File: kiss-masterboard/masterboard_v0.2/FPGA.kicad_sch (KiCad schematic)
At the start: 68 parts, among them J10 CRESET, J11 Jumper, J12 Jumper, J13 Conn_02x08_Odd_Even, J14 Conn_02x08_Odd_Even, J15 jmp, J16 jmp, J8 Jumper, J9 jmp, U12 1V2, U13 SN74LVC8T245, U14 W25Q, U17 12MHz, U2 SN74LVC8T245, U3 3.3V, U4 ICE40UP5k-SG48, U5 SN74LVC8T245

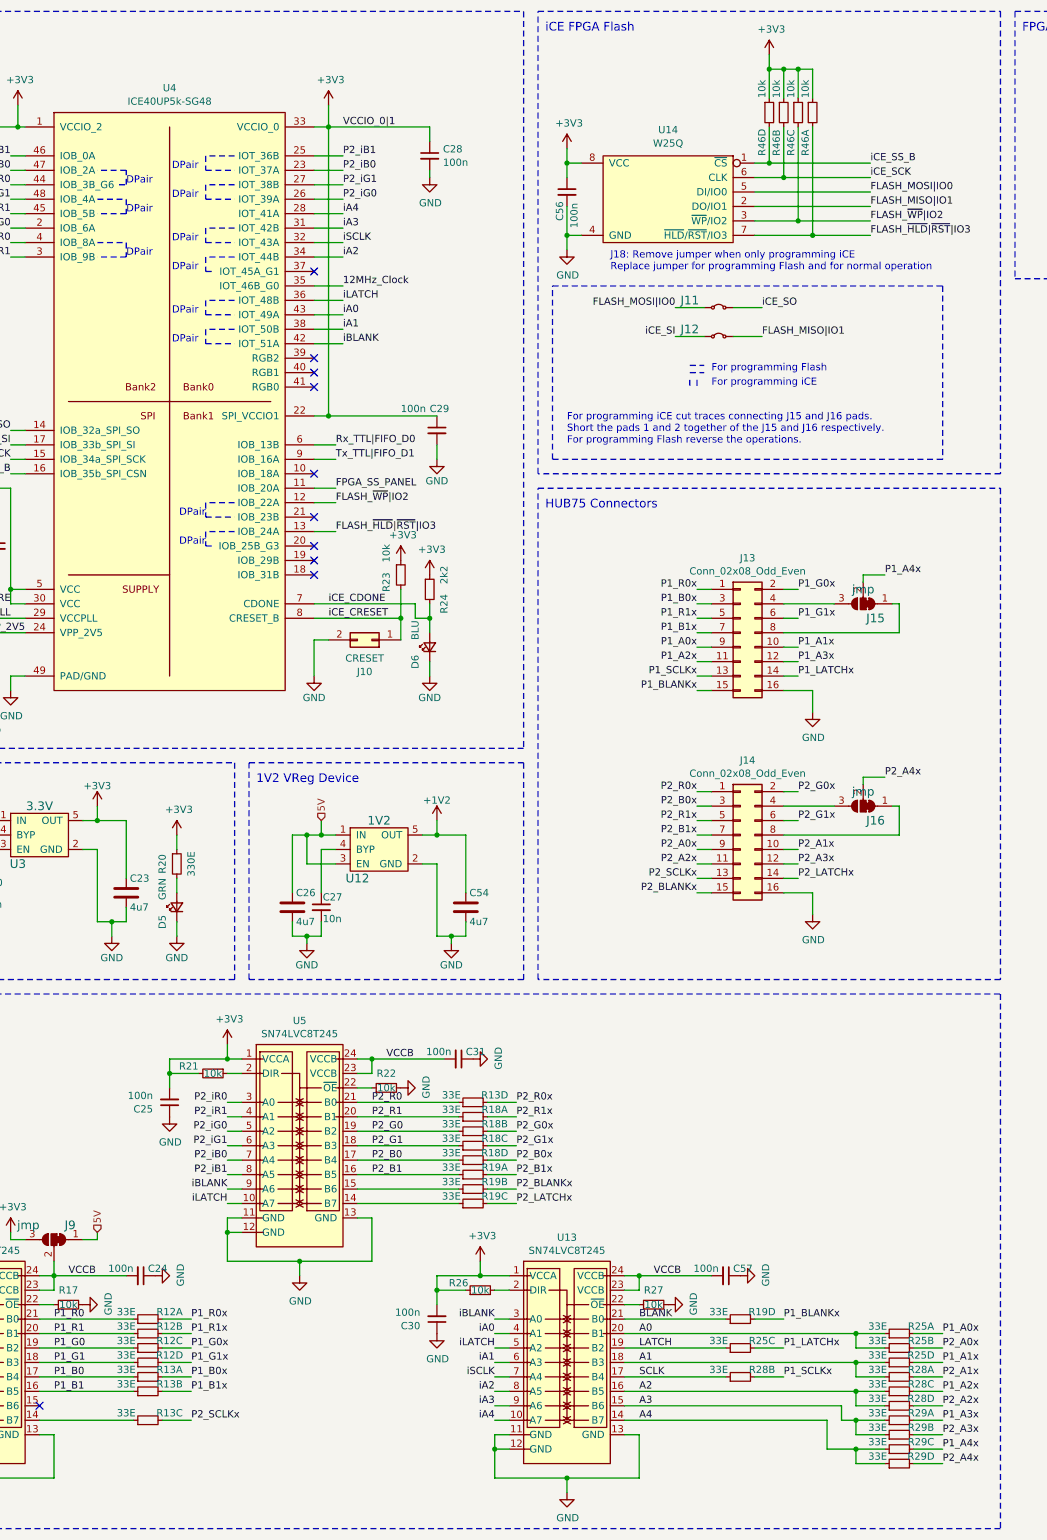
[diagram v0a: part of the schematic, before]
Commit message: replaced resistor array with normal resistors
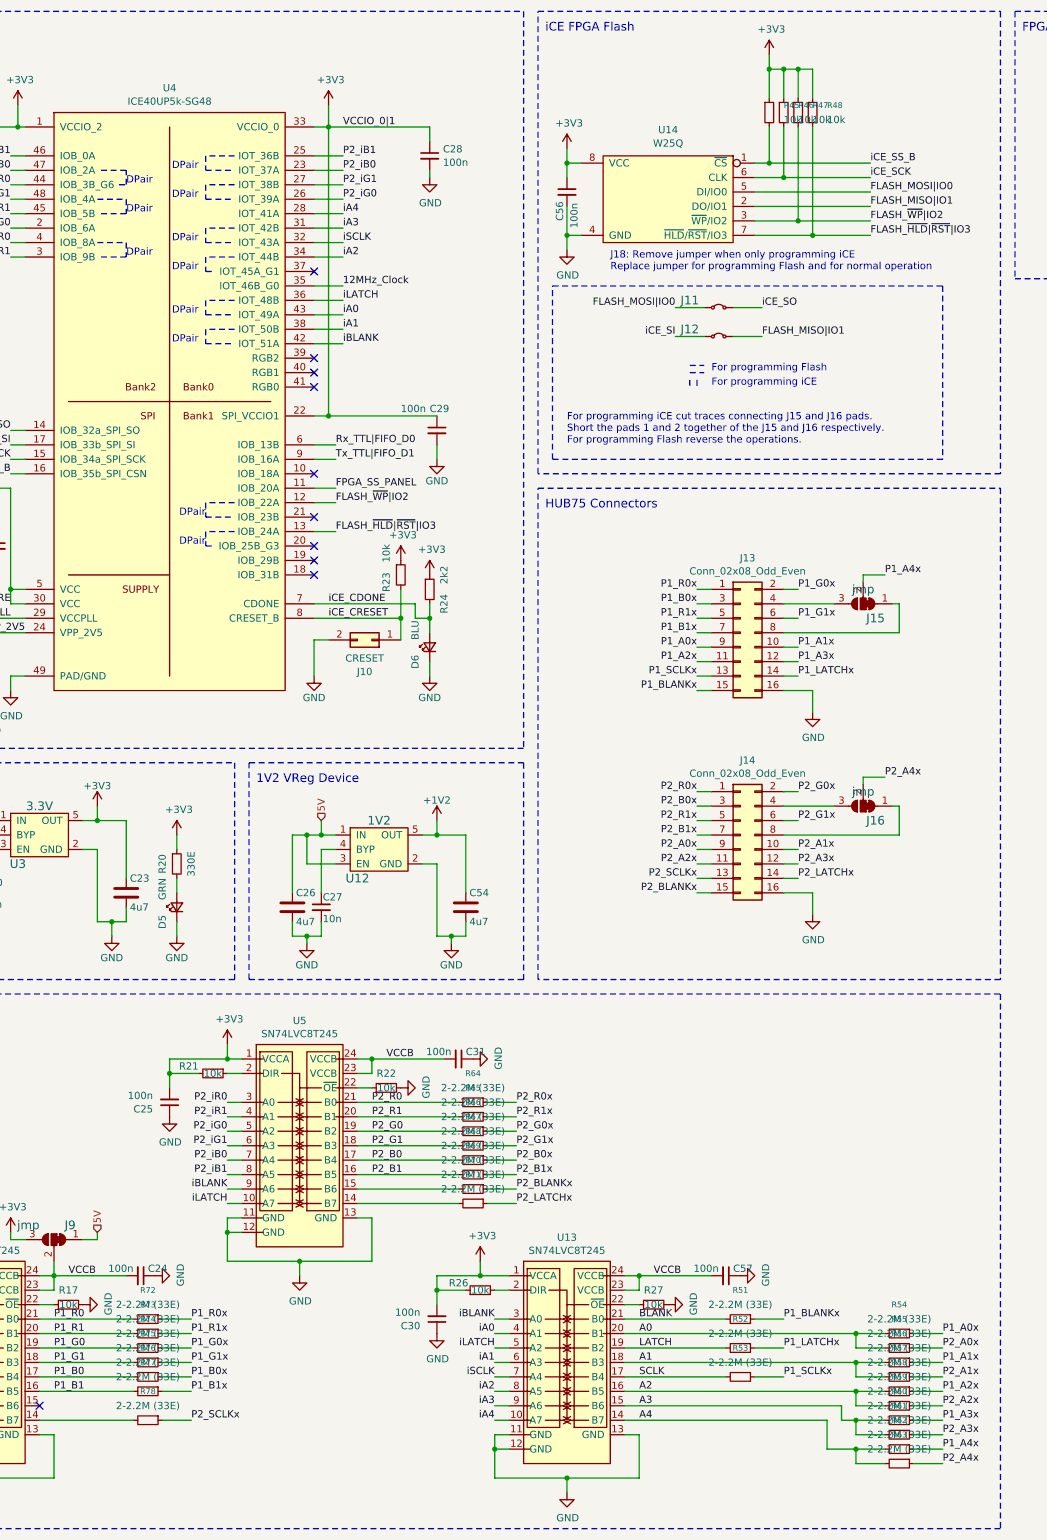
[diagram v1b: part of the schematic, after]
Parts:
- removed R12, R13, R18, R19, R25, R28, R29: 33E, pkl_dipol:R_Array_Convex_4x0402, symbol pkl_device:pkl_R4_Small
- removed R46: 10k, pkl_dipol:R_Array_Convex_4x0402, symbol pkl_device:pkl_R4_Small
- added R45, R46, R47, R48: 10k, Resistor_SMD:R_0603_1608Metric, symbol Device:R_Small
- added R51, R52, R53, R54, R55, R56, R57, R58, R59, R60, R61, R62, R63, R64, R65, R66, R67, R68, R69, R70, R71, R72, R73, R74, R75, R76, R77, R78: 2-2.2M (33E), pkl_dipol:R_0402, symbol Device:R_Small
- C56: footprint Capacitor_SMD:C_0402_1005Metric -> Capacitor_SMD:C_0603_1608Metric
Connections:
- net +3V3: now also R45.1, R46.1, R47.1, R48.1
- net A0: now also R54.2, R55.2
- net A1: now also R56.2, R57.2
- net A2: now also R58.2, R59.2
- net A3: now also R60.2, R61.2
- net A4: now also R62.2, R63.2
- net BLANK: now also R51.2
- net FLASH_~{HLD}|~{RST}|IO3: now also R48.2
- net FLASH_~{WP}|IO2: now also R47.2
- net LATCH: now also R52.2
- net P1_A0x: now also R54.1
- net P1_A1x: now also R56.1
- net P1_A2x: now also R58.1
- net P1_A3x: now also R60.1
- net P1_A4x: now also R62.1
- net P1_B0: now also R76.2
- net P1_B0x: now also R76.1
- net P1_B1: now also R77.2
- net P1_B1x: now also R77.1
- net P1_BLANKx: now also R51.1
- net P1_G0: now also R74.2
- net P1_G0x: now also R74.1
- net P1_G1: now also R75.2
- net P1_G1x: now also R75.1
- net P1_LATCHx: now also R52.1
- net P1_R0: now also R72.2
- net P1_R0x: now also R72.1
- net P1_R1: now also R73.2
- net P1_R1x: now also R73.1
- net P1_SCLKx: now also R53.1
- net P2_A0x: now also R55.1
- net P2_A1x: now also R57.1
- net P2_A2x: now also R59.1
- net P2_A3x: now also R61.1
- net P2_A4x: now also R63.1
- net P2_B0: now also R68.2
- net P2_B0x: now also R68.1
- net P2_B1: now also R69.2
- net P2_B1x: now also R69.1
- net P2_BLANKx: now also R70.1
- net P2_G0: now also R66.2
- net P2_G0x: now also R66.1
- net P2_G1: now also R67.2
- net P2_G1x: now also R67.1
- net P2_LATCHx: now also R71.1
- net P2_R0: now also R64.2
- net P2_R0x: now also R64.1
- net P2_R1: now also R65.2
- net P2_R1x: now also R65.1
- net P2_SCLKx: now also R78.1
- net SCK: now also R46.2
- net SCLK: now also R53.2
- net SS_FLASH: now also R45.2
- net at U2.14 (B7): now also R78.2
- net at U5.15 (B6): now also R70.2
- net at U5.14 (B7): now also R71.2

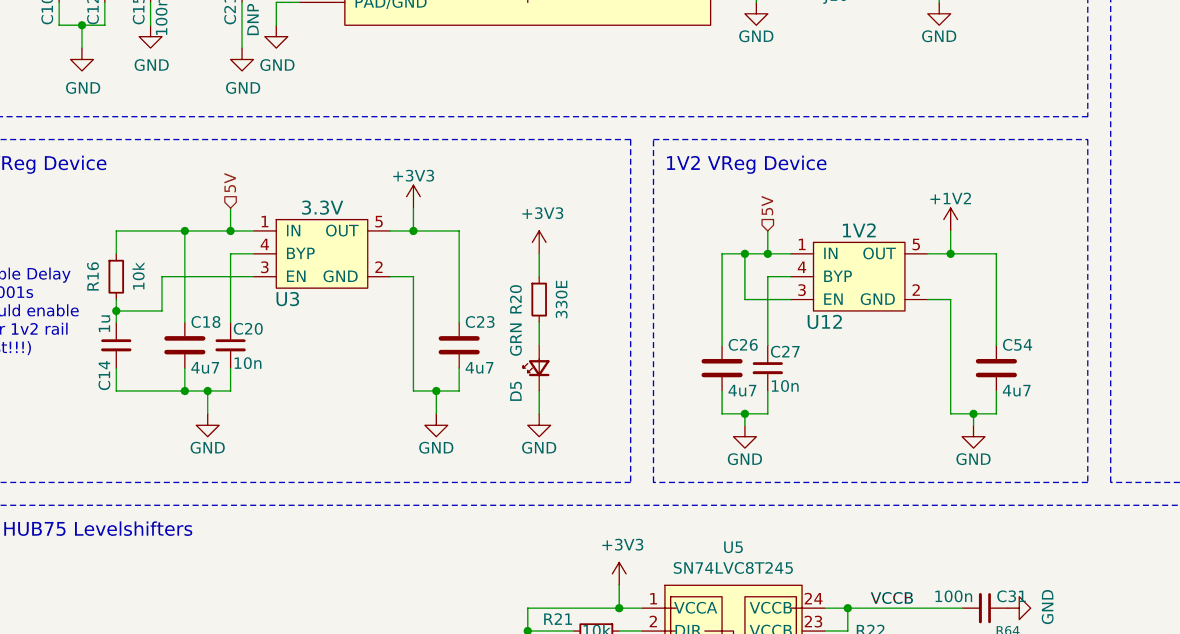
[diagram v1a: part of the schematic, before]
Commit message: replaced symbosl with standart symbols and reduced DRC errorsMAX98357A and TLV75709PDBV symbols
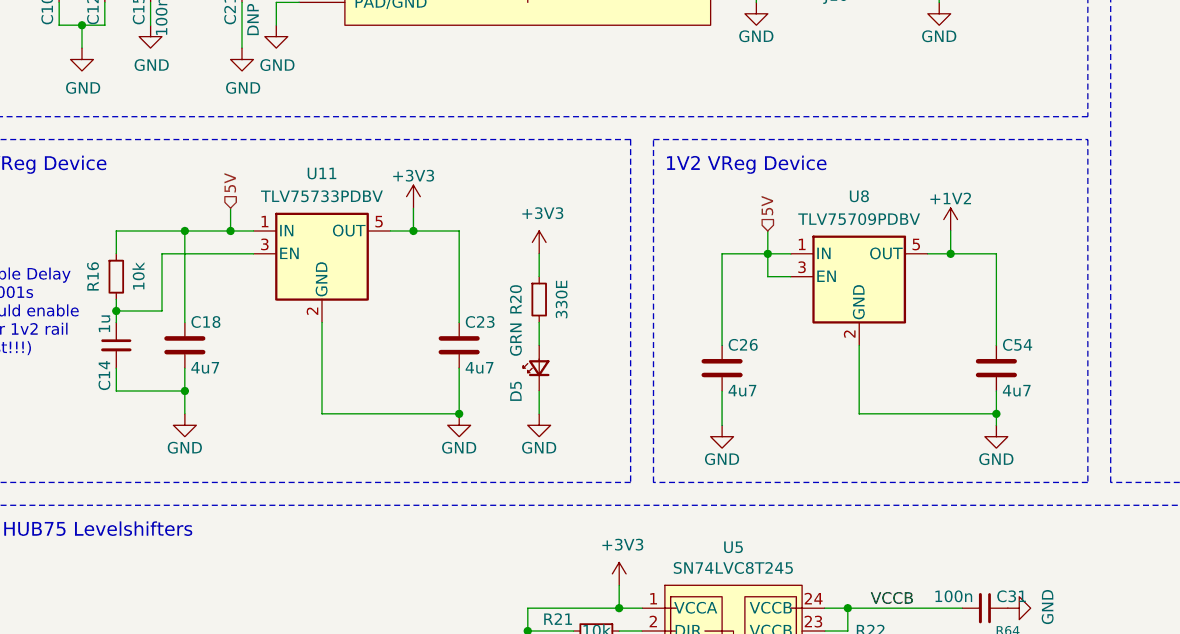
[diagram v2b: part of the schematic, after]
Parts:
- removed C20, C27: 10n, Capacitor_SMD:C_0402_1005Metric, symbol Device:C_Small
- removed U12: 1V2, pkl_housings_sot:SOT-23-5, symbol pkl_device:pkl_VREG_5PIN_FIXED
- removed U3: 3.3V, pkl_housings_sot:SOT-23-5, symbol pkl_device:pkl_VREG_5PIN_FIXED
- added U11: TLV75733PDBV, Package_TO_SOT_SMD:SOT-23-5, symbol Regulator_Linear:TLV75733PDBV
- added U8: TLV75709PDBV, Package_TO_SOT_SMD:SOT-23-5, symbol Regulator_Linear:TLV75709PDBV
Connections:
- net +1V2: now also U8.5 (OUT)
- net +3V3: now also U11.5 (OUT)
- net 5V: now also U11.1 (IN), U8.1 (IN), U8.3 (EN)
- net GND: now also U11.2 (GND), U8.2 (GND)
- net at C14.1, R16.2: now also U11.3 (EN)

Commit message: Fix DRC issues
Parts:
- J11, J12: footprint pkl_jumpers:J_NC_0603_15 -> Jumper:SolderJumper-2_P1.3mm_Bridged2Bar_Pad1.0x1.5mm
- J9: footprint pkl_jumpers:J_NCNO_0903_30 -> Jumper:SolderJumper-3_P1.3mm_Bridged12_Pad1.0x1.5mm
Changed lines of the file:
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@@
 			)
 		)
-		(property "Footprint" "pkl_jumpers:J_NCNO_0903_30"
+		(property "Footprint" "Jumper:SolderJumper-3_P1.3mm_Bridged12_Pad1.0x1.5mm"
 			(at 60.96 231.14 0)
 			(hide yes)
@@
 			)
 		)
-		(property "Footprint" "pkl_jumpers:J_NC_0603_15"
+		(property "Footprint" "Jumper:SolderJumper-2_P1.3mm_Bridged2Bar_Pad1.0x1.5mm"
 			(at 177.8 67.31 0)
 			(hide yes)
@@
 			)
 		)
-		(property "Footprint" "pkl_jumpers:J_NC_0603_15"
+		(property "Footprint" "Jumper:SolderJumper-2_P1.3mm_Bridged2Bar_Pad1.0x1.5mm"
 			(at 177.8 72.39 0)
 			(hide yes)

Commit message: Added IMU, routed extension layer, switched battery polarity
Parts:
- removed J9: jmp, Jumper:SolderJumper-3_P1.3mm_Bridged12_Pad1.0x1.5mm, symbol Jumper:SolderJumper_3_Bridged12
- C11, C12, C15, C16, C19, C24, C25, C28, C29, C30, C31, C56, C57, C61, C9: value 100n -> 100nF
- C14, C17, C8: value 1u -> 1uF
- R14: value 100E -> 100
- R20: value 330E -> 330
- R24: value 2k2 -> 2.2k
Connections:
- net VCCB is gone; now on net 5V: C24.2, C31.2, C57.2, U13.23 (VCCB), U13.24 (VCCB), U2.23 (VCCB), U2.24 (VCCB), U5.23 (VCCB), U5.24 (VCCB)
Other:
- note added: "For programming iCE cut traces connecting J11 and J12 pads. Short the pads 1 and 2 together of the J11 and J12 respectively. For programming Flash reverse the operations."
- note removed: "For programming iCE cut traces connecting J15 and J16 pads. Short the pads 1 and 2 together of the J15 and J16 respectively. For programming Flash reverse the operations."
